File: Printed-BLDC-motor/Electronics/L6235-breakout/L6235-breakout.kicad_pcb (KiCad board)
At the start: 2 copper layers, 31 parts, among them J1 CONTROL, J2 HALL, J3 MOTOR, J4 5V, J5 PWR, U1 L6235PD

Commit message: Gearbox and L6235 updates.
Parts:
- removed C9: C, Capacitor_SMD:C_0805_2012Metric
- removed D3: 1N4148, Diode_SMD:D_0805_2012Metric
- added R13: 1R, Resistor_SMD:R_0805_2012Metric, F.Cu at (41.9, 189.7)
- C3: footprint Capacitor_THT:CP_Radial_D6.3mm_P2.50mm -> Capacitor_THT:C_Radial_D8.0mm_H7.0mm_P3.50mm
- R5: value 0.33R -> 1R
- R7: value R -> 1R
- moved U1 309.9 mm to (31.6, 177.3)
- moved R4 301.3 mm to (22.5, 182.9), turned to 270 degrees
- moved C6 300.2 mm to (20.5, 182.9), turned to 270 degrees
- moved J3 298.7 mm to (24.2, 188.4)
- moved J2 297.0 mm to (11.6, 183.2)
- moved R7 294.8 mm to (41.9, 187.7), turned to 180 degrees
- moved R11 293.4 mm to (16.4, 176.2), turned to 90 degrees
- moved C4 292.1 mm to (13.0, 180.0), turned to 180 degrees
- moved C7 290.1 mm to (16.6, 166.6), turned to 270 degrees
- moved R12 289.6 mm to (19.7, 176.6), turned to 270 degrees
- moved R10 289.1 mm to (16.8, 180.0)
- moved D1 287.1 mm to (19.8, 167.3)
- moved C8 286.9 mm to (20.5, 173.3), turned to 180 degrees
- moved R5 284.5 mm to (41.9, 185.7), turned to 180 degrees
- moved C3 284.2 mm to (9.86, 165.1), turned to 270 degrees
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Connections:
- C3 pad 1: (no net) -> VSS
- C3 pad 2: (no net) -> GND
- R5 pad 2: Net-(R5-Pad2) -> Net-(R13-Pad2)
- R7 pad 1: Net-(R7-Pad1) -> GND
- R7 pad 2: Net-(R7-Pad2) -> Net-(R13-Pad2)
- U1 pad 12: Net-(R5-Pad2) -> Net-(R13-Pad2)
- U1 pad 25: Net-(R5-Pad2) -> Net-(R13-Pad2)
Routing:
- net Net-(C7-Pad2): track 0.00 -> 72.9 mm
- net TACHO: track 0.00 -> 72.5 mm
- net F-R: track 0.00 -> 50.6 mm
- net VSS: track 0.00 -> 40.1 mm
- net HALL2: track 0.00 -> 39.4 mm
- net Net-(R13-Pad2): track 0.00 -> 34.5 mm
- net Net-(J1-Pad2): track 0.00 -> 25.4 mm
- net ENABLE: track 0.00 -> 23.7 mm
- net BRAKE: track 0.00 -> 19.0 mm
- net VREF: track 0.00 -> 18.4 mm
- net HALL1: track 0.00 -> 18.2 mm
- net +5V: track 0.00 -> 16.2 mm
- net PHASE1: track 0.00 -> 12.4 mm
- net Net-(C6-Pad1): track 0.00 -> 6.54 mm
- net Net-(D1-Pad1): track 0.00 -> 6.24 mm
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- added copper zone on F.Cu, net GND
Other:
- board outline added: 56.9 x 39.2 mm

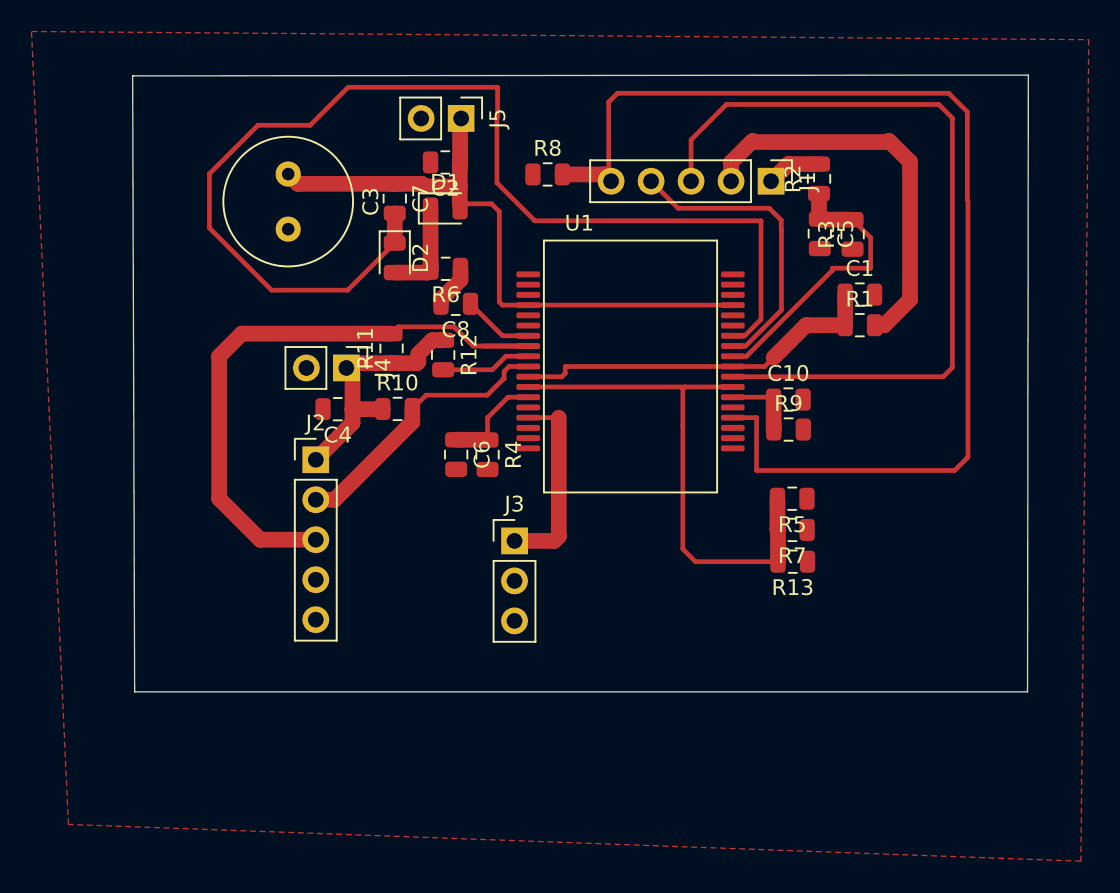
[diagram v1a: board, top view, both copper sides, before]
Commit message: Latest version of Sally's L6235-breakout
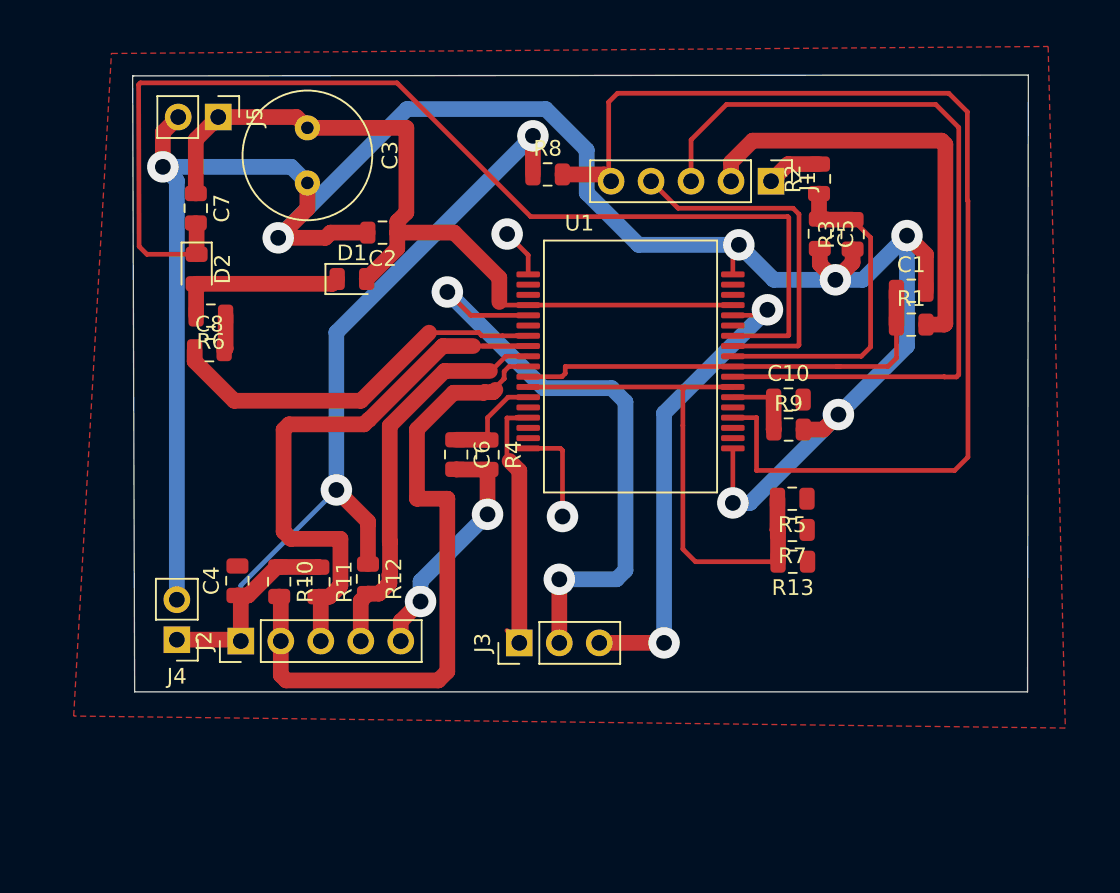
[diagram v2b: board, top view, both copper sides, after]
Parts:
- moved J4 20.3 mm to (2.78, 194.7), turned to 180 degrees
- moved C8 15.9 mm to (4.85, 176.3), turned to 0 degrees
- moved R11 15.5 mm to (11.8, 191.0), turned to 270 degrees
- moved J5 15.4 mm to (5.41, 161.5)
- moved R6 15.2 mm to (4.94, 174.1)
- moved R12 15.0 mm to (14.9, 190.8)
- moved R10 13.3 mm to (9.28, 191.0), turned to 270 degrees
- moved C7 12.7 mm to (3.99, 167.2)
- moved C4 12.6 mm to (6.63, 190.9), turned to 90 degrees
- moved D2 12.6 mm to (4.04, 171.1)
- moved J2 12.5 mm to (6.85, 194.7), turned to 90 degrees
- moved D1 7.43 mm to (13.9, 171.7)
- moved J3 6.48 mm to (24.5, 194.9), turned to 90 degrees
- moved C2 5.98 mm to (15.8, 168.8)
- moved C1 3.27 mm to (49.4, 172.5)
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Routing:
- net GND: track 0.00 -> 165.5 mm, vias 0 -> 11
- net +5V: track 16.2 -> 60.8 mm, vias 0 -> 2
- net PHASE2: track 0.09 -> 39.1 mm, vias 0 -> 2
- net PHASE3: track 0.00 -> 30.3 mm, vias 0 -> 2
- net HALL1: track 18.2 -> 42.6 mm
- net Net-(C8-Pad1): track 5.26 -> 25.6 mm
- net HALL3: track 6.00 -> 25.5 mm
- net VSS: track 40.1 -> 52.4 mm
- net ENABLE: track 23.7 -> 28.6 mm
- net Net-(D1-Pad1): track 6.24 -> 11.1 mm
- net PHASE1: track 12.4 -> 17.1 mm
- net BRAKE: track 19.0 -> 22.8 mm
- net VREF: track 18.4 -> 21.3 mm
- net Net-(J1-Pad2): track 25.4 -> 28.1 mm
- net HALL2: track 39.4 -> 37.8 mm
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
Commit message: Latest BLDC driver PCB.
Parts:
- removed J4: 5V, Connector_PinHeader_2.54mm:PinHeader_1x02_P2.54mm_Vertical
- added C9: 100u, Capacitor_THT:C_Radial_D8.0mm_H7.0mm_P3.50mm, F.Cu at (15.2, 160.8)
- added H1: MountingHole, MountingHole:MountingHole_3.2mm_M3, F.Cu at (52.0, 186.0)
- added H2: MountingHole, MountingHole:MountingHole_3.2mm_M3, F.Cu at (52.0, 151.0)
- added H3: MountingHole, MountingHole:MountingHole_3.2mm_M3, F.Cu at (5.00, 163.0)
- added H4: MountingHole, MountingHole:MountingHole_3.2mm_M3, F.Cu at (5.00, 186.0)
- added IC1: 7805DT, Package_TO_SOT_SMD:TO-252-2, F.Cu at (11.0, 152.2)
- moved C4 33.9 mm to (7.00, 157.0), turned to 0 degrees
- moved J2 28.9 mm to (15.6, 167.2), turned to 0 degrees
- moved C3 25.8 mm to (36.5, 157.7), turned to 90 degrees
- moved J5 25.0 mm to (30.1, 157.6), turned to 180 degrees
- moved C7 24.9 mm to (23.8, 152.1), turned to 180 degrees
- moved D2 24.7 mm to (20.5, 152.7)
- moved R7 23.7 mm to (20.2, 178.3), turned to 0 degrees
- moved R13 22.8 mm to (20.2, 182.5), turned to 0 degrees
- moved R5 22.3 mm to (20.2, 180.4), turned to 0 degrees
- moved R8 20.7 mm to (42.7, 177.7), turned to 90 degrees
- moved R11 19.8 mm to (11.3, 171.2), turned to 0 degrees
- moved R10 19.1 mm to (20.2, 175.4), turned to 0 degrees
- moved C8 16.8 mm to (19.3, 167.7)
- moved R6 16.7 mm to (19.4, 165.6)
- moved R12 16.5 mm to (11.7, 174.7), turned to 0 degrees
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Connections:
- U1 pad 25: Net-(R13-Pad2) -> Net-(U1-Pad25)
- U1 pad 33: VSS -> Net-(U1-Pad33)
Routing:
- net GND: track 165.5 -> 36.9 mm, vias 11 -> 60
- net TACHO: track 72.5 -> 12.3 mm
- net F-R: track 51.3 -> 11.2 mm
- net PHASE3: track 30.3 -> 58.2 mm, vias 2 -> 0
- net Net-(C7-Pad2): track 72.1 -> 46.0 mm
- net Net-(J1-Pad2): track 28.1 -> 4.17 mm
- net HALL2: track 37.8 -> 14.3 mm
- net +5V: track 60.8 -> 82.4 mm, vias 2 -> 3
- net Net-(R13-Pad2): track 34.5 -> 14.2 mm
- net Net-(C8-Pad1): track 25.6 -> 7.05 mm
- net HALL3: track 25.5 -> 14.9 mm
- net BRAKE: track 22.8 -> 32.2 mm, vias 0 -> 1
- net PHASE2: track 39.1 -> 30.2 mm, vias 2 -> 1
- net VREF: track 21.3 -> 12.8 mm
- net HALL1: track 42.6 -> 51.0 mm
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- added copper zone on B.Cu, net GND
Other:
- board size 56.9 x 39.2 mm -> 55 x 43 mm
- board text added: "BLDC Motor Controller Version 1"
- board text added: "RepRap Ltd reprapltd.com Design: S Bowyer Licence: GPL"

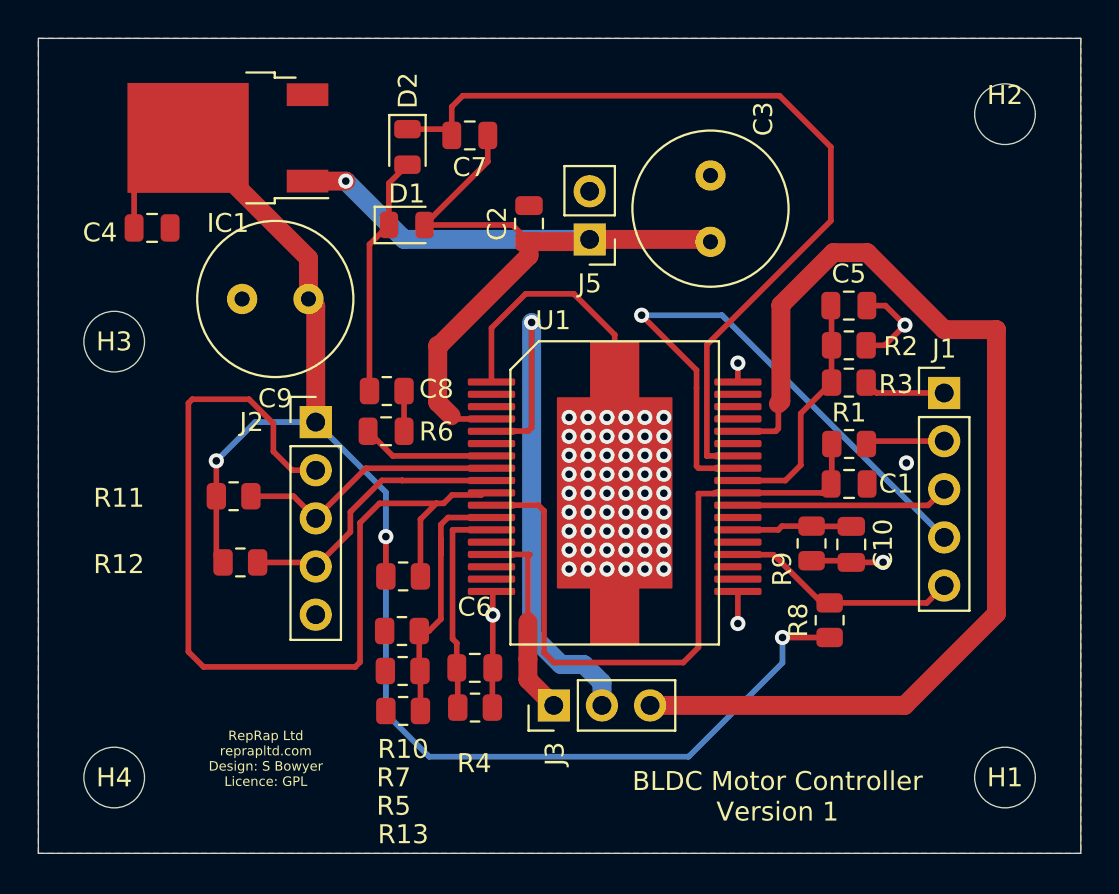
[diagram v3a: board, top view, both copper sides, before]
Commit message: Footprint of TO-220 7805 corrected.
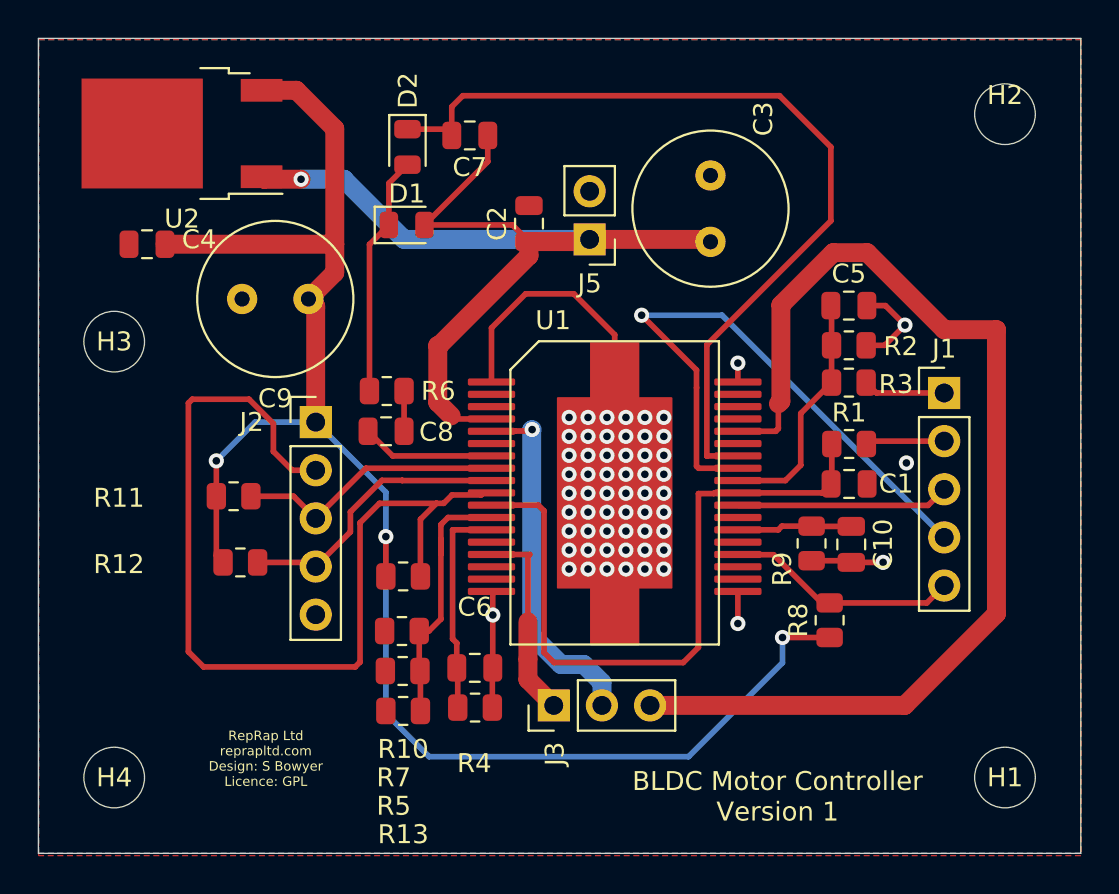
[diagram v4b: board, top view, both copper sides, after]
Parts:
- removed IC1: 7805DT, Package_TO_SOT_SMD:TO-252-2
- added U2: L7805, Package_TO_SOT_SMD:TO-252-2, F.Cu at (8.58, 152.0)
- moved C4 0.90 mm to (6.73, 157.9), turned to 180 degrees
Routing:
- net PHASE2: track 30.2 -> 19.0 mm
- net +5V: track 82.4 -> 88.5 mm
- net VSS: track 51.6 -> 54.2 mm

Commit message: Controller PCB updated to Version 2.
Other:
- board text added: "BLDC Motor Controller Version 2"
- board text removed: "BLDC Motor Controller Version 1"

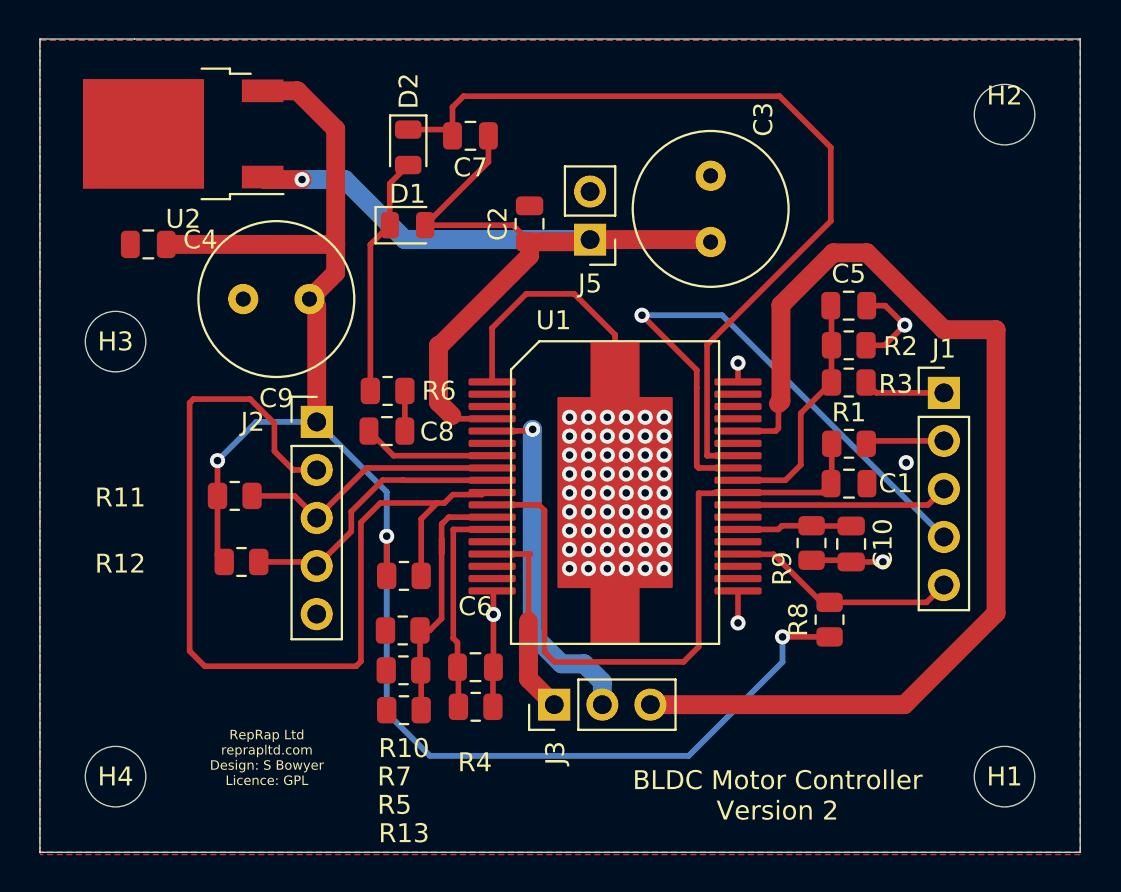
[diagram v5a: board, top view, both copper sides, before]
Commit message: Added ground reference to control connector.
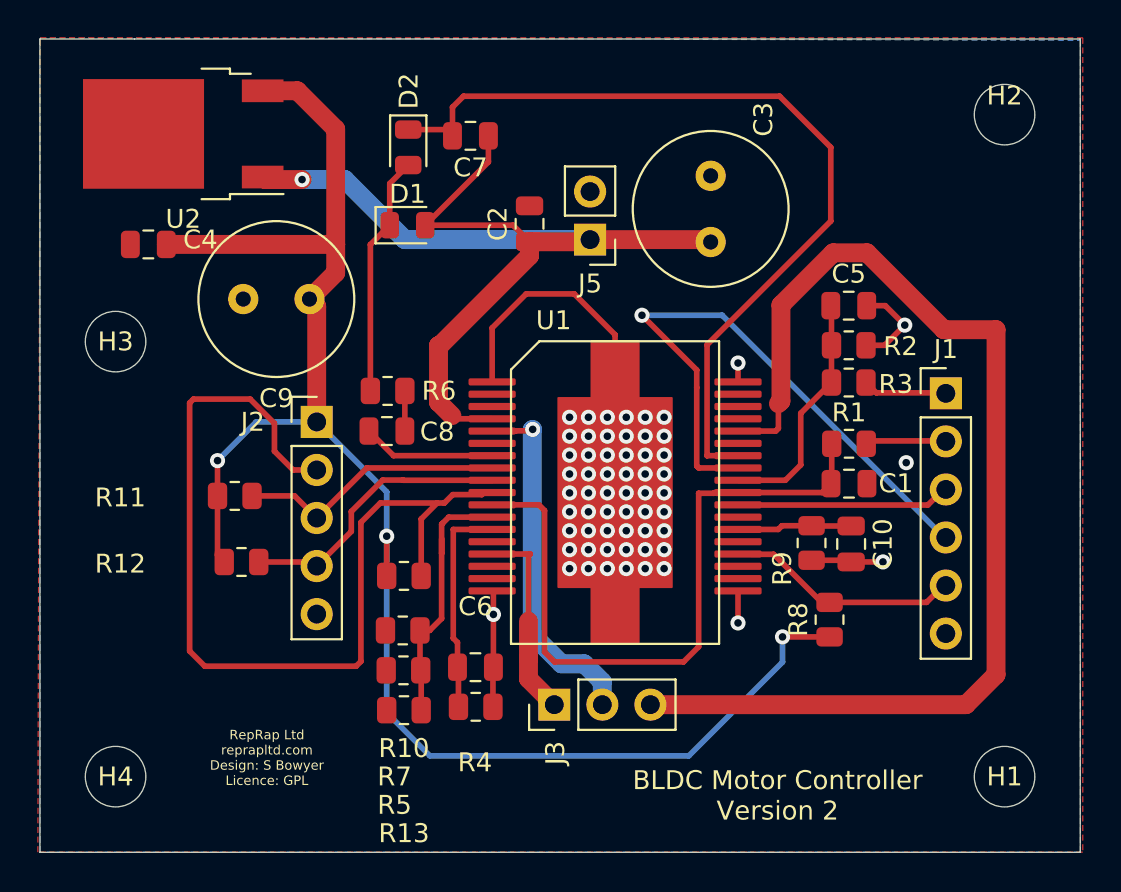
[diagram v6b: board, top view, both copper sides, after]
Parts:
- J1: value CONTROL -> Conn_01x06_Male; footprint Connector_PinHeader_2.54mm:PinHeader_1x05_P2.54mm_Vertical -> Connector_PinHeader_2.54mm:PinHeader_1x06_P2.54mm_Vertical
- moved J1 0.10 mm to (48.9, 165.7)
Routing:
- net PHASE3: track 58.2 -> 60.1 mm
